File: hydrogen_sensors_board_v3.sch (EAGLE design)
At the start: 97 parts, among them CN1 1X4-CLEANBIG, IC1 317T, IC2 LM741D, U1 ATMEGA328P_TQFP, Y1 16MHz

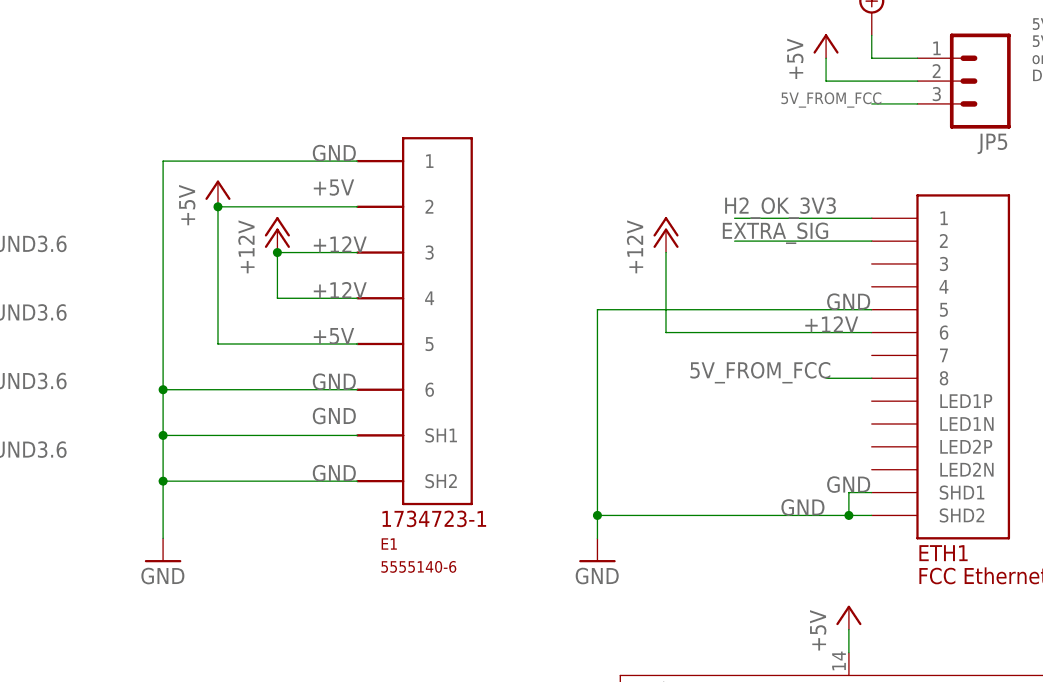
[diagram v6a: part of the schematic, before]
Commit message: updated rj 11 part. added signals to ethernet connector
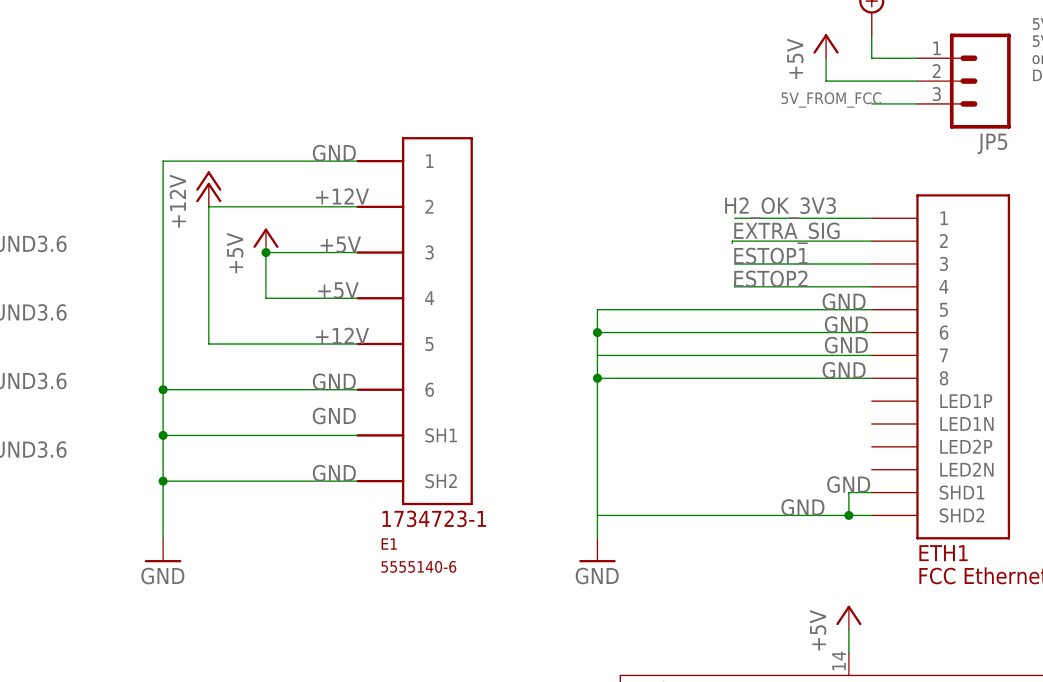
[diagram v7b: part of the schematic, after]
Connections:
- net +12V: now also E1.2, E1.5; no longer E1.3, E1.4, ETH1.6
- net +5V: now also E1.3, E1.4; no longer E1.2, E1.5
- net 5V_FROM_FCC: no longer ETH1.8
- net ESTOP1: now also ETH1.3
- net ESTOP2: now also ETH1.4
- net GND: now also ETH1.6, ETH1.7, ETH1.8
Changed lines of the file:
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@@
 <?xml version="1.0" encoding="utf-8"?>
 <!DOCTYPE eagle SYSTEM "eagle.dtd">
-<eagle version="7.6.0">
+<eagle version="9.1.0">
 <drawing>
 <settings>
 <setting alwaysvectorfont="no"/>
+<setting keepoldvectorfont="yes"/>
 <setting verticaltext="up"/>
 </settings>
-<grid distance="0.1" unitdist="inch" unit="inch" style="lines" multiple="1" display="no" altdistance="0.01" altunitdist="inch" altunit="inch"/>
+<grid distance="0.01" unitdist="inch" unit="inch" style="lines" multiple="1" display="no" altdistance="0.01" altunitdist="inch" altunit="inch"/>
 <layers>
 <layer number="1" name="Top" color="4" fill="1" visible="no" active="no"/>
@@
 <part name="P+14" library="supply1" deviceset="+5V" device=""/>
 <part name="P+15" library="supply1" deviceset="+5V" device=""/>
-<part name="P+17" library="supply1" deviceset="+12V" device=""/>
 <part name="GND14" library="SparkFun" deviceset="GND" device=""/>
-<part name="P+18" library="supply1" deviceset="+5V" device=""/>
 <part name="P+19" library="supply1" deviceset="+12V" device=""/>
 <part name="GND15" library="supply1" deviceset="GND" device=""/>
@@
 <part name="D1" library="adafruit" deviceset="DIODE" device="SMA" value="S1GTR"/>
 <part name="D2" library="adafruit" deviceset="DIODE" device="SMA" value="S1GTR"/>
+<part name="P+23" library="supply1" deviceset="+5V" device=""/>
 </parts>
 <sheets>
@@
 <instance part="P+14" gate="1" x="509.778" y="155.194"/>
 <instance part="P+15" gate="1" x="509.27" y="139.7"/>
-<instance part="P+17" gate="1" x="434.34" y="146.05"/>
 <instance part="GND14" gate="1" x="378.46" y="109.22"/>
-<instance part="P+18" gate="1" x="384.556" y="151.384"/>
-<instance part="P+19" gate="1" x="391.16" y="146.05"/>
+<instance part="P+19" gate="1" x="383.54" y="151.13"/>
 <instance part="GND15" gate="1" x="63.5" y="270.256"/>
 <instance part="GND16" gate="1" x="50.8" y="295.656"/>
@@
 <attribute name="VALUE" x="54.864" y="340.614" size="1.27" layer="96"/>
 </instance>
+<instance part="P+23" gate="1" x="389.89" y="146.05"/>
 </instances>
 <busses>
@@
 <wire x1="463.55" y1="356.87" x2="454.66" y2="356.87" width="0.1524" layer="91"/>
 <wire x1="454.66" y1="356.87" x2="454.66" y2="360.68" width="0.1524" layer="91"/>
-</segment>
-<segment>
-<pinref part="P+18" gate="1" pin="+5V"/>
-<wire x1="384.556" y1="148.844" x2="384.556" y2="148.59" width="0.1524" layer="91"/>
-<pinref part="E1" gate="G$1" pin="5"/>
-<label x="394.97" y="133.35" size="1.778" layer="95"/>
-<wire x1="384.556" y1="148.59" x2="384.556" y2="133.35" width="0.1524" layer="91"/>
-<wire x1="384.556" y1="133.35" x2="400.05" y2="133.35" width="0.1524" layer="91"/>
-<pinref part="E1" gate="G$1" pin="2"/>
-<label x="394.97" y="149.86" size="1.778" layer="95"/>
-<wire x1="400.05" y1="148.59" x2="384.556" y2="148.59" width="0.1524" layer="91"/>
-<junction x="384.556" y="148.59"/>
 </segment>
 <segment>
@@
 <junction x="53.34" y="113.284"/>
 </segment>
+<segment>
+<pinref part="E1" gate="G$1" pin="3"/>
+<wire x1="389.89" y1="143.51" x2="400.05" y2="143.51" width="0.1524" layer="91"/>
+<pinref part="E1" gate="G$1" pin="4"/>
+<wire x1="400.05" y1="138.43" x2="389.89" y2="138.43" width="0.1524" layer="91"/>
+<wire x1="389.89" y1="138.43" x2="389.89" y2="143.51" width="0.1524" layer="91"/>
+<pinref part="P+23" gate="1" pin="+5V"/>
+<junction x="389.89" y="143.51"/>
+<label x="395.732" y="143.51" size="1.778" layer="95"/>
+<label x="395.478" y="138.43" size="1.778" layer="95"/>
+</segment>
 </net>
 <net name="GND" class="0">
@@
 <segment>
 <pinref part="GND7" gate="1" pin="GND"/>
-<wire x1="426.72" y1="137.16" x2="426.72" y2="114.3" width="0.1524" layer="91"/>
+<pinref part="ETH1" gate="G$1" pin="SHD1"/>
 <wire x1="426.72" y1="114.3" x2="426.72" y2="111.76" width="0.1524" layer="91"/>
-<pinref part="ETH1" gate="G$1" pin="SHD1"/>
 <wire x1="457.2" y1="116.84" x2="454.66" y2="116.84" width="0.1524" layer="91"/>
 <wire x1="454.66" y1="116.84" x2="454.66" y2="114.3" width="0.1524" layer="91"/>
@@
 <junction x="454.66" y="114.3"/>
 <wire x1="454.66" y1="114.3" x2="426.72" y2="114.3" width="0.1524" layer="91"/>
-<junction x="426.72" y="114.3"/>
+<label x="452.12" y="116.84" size="1.778" layer="95"/>
+<label x="447.04" y="114.3" size="1.778" layer="95"/>
+<pinref part="ETH1" gate="G$1" pin="8"/>
+<wire x1="457.2" y1="129.54" x2="426.72" y2="129.54" width="0.1524" layer="91"/>
+<wire x1="426.72" y1="129.54" x2="426.72" y2="114.3" width="0.1524" layer="91"/>
+<pinref part="ETH1" gate="G$1" pin="7"/>
+<wire x1="457.2" y1="132.08" x2="426.72" y2="132.08" width="0.1524" layer="91"/>
+<junction x="426.72" y="129.54"/>
+<pinref part="ETH1" gate="G$1" pin="6"/>
+<wire x1="426.72" y1="132.08" x2="426.72" y2="129.54" width="0.1524" layer="91"/>
+<wire x1="457.2" y1="134.62" x2="426.72" y2="134.62" width="0.1524" layer="91"/>
+<wire x1="426.72" y1="134.62" x2="426.72" y2="132.08" width="0.1524" layer="91"/>
 <pinref part="ETH1" gate="G$1" pin="5"/>
 <wire x1="457.2" y1="137.16" x2="426.72" y2="137.16" width="0.1524" layer="91"/>
-<label x="452.12" y="137.16" size="1.778" layer="95"/>
-<label x="452.12" y="116.84" size="1.778" layer="95"/>
-<label x="447.04" y="114.3" size="1.778" layer="95"/>
+<wire x1="426.72" y1="137.16" x2="426.72" y2="134.62" width="0.1524" layer="91"/>
+<junction x="426.72" y="134.62"/>
+<label x="451.612" y="137.16" size="1.778" layer="95"/>
+<label x="451.866" y="134.62" size="1.778" layer="95"/>
+<label x="451.866" y="132.334" size="1.778" layer="95"/>
+<label x="451.612" y="129.54" size="1.778" layer="95"/>
 </segment>
 <segment>
@@
 <net name="EXTRA_SIG" class="0">
 <segment>
-<pinref part="ETH1" gate="G$1" pin="2"/>
-<label x="440.436" y="145.034" size="1.778" layer="95"/>
-<wire x1="457.2" y1="144.78" x2="441.96" y2="144.78" width="0.1524" layer="91"/>
-</segment>
-<segment>
 <pinref part="R25" gate="G$1" pin="2"/>
 <pinref part="R26" gate="G$1" pin="2"/>
@@
 <label x="485.14" y="334.264" size="1.27" layer="95"/>
 </segment>
+<segment>
+<pinref part="ETH1" gate="G$1" pin="2"/>
+<wire x1="457.2" y1="144.78" x2="441.706" y2="144.78" width="0.1524" layer="91"/>
+<wire x1="441.706" y1="144.78" x2="441.706" y2="144.526" width="0.1524" layer="91"/>
+<label x="441.706" y="145.034" size="1.778" layer="95"/>
+</segment>
 </net>
 <net name="RXD" class="0">
@@
 <label x="408.94" y="88.9" size="1.016" layer="95"/>
 </segment>
+<segment>
+<pinref part="ETH1" gate="G$1" pin="3"/>
+<wire x1="457.2" y1="142.24" x2="441.96" y2="142.24" width="0.1524" layer="91"/>
+<label x="441.706" y="142.24" size="1.778" layer="95"/>
+</segment>
 </net>
 <net name="ESTOP2" class="0">
@@
 <pinref part="U$8" gate="G$1" pin="1B"/>
 <label x="408.94" y="86.36" size="1.016" layer="95"/>
+</segment>
+<segment>
+<pinref part="ETH1" gate="G$1" pin="4"/>
+<wire x1="457.2" y1="139.7" x2="441.96" y2="139.7" width="0.1524" layer="91"/>
+<wire x1="441.96" y1="139.7" x2="441.96" y2="140.208" width="0.1524" layer="91"/>
+<label x="441.706" y="139.7" size="1.778" layer="95"/>
 </segment>
 </net>
@@
 <junction x="510.54" y="109.22"/>
 <pinref part="P+12" gate="1" pin="+12V"/>
-</segment>
-<segment>
-<pinref part="ETH1" gate="G$1" pin="6"/>
-<label x="449.58" y="134.62" size="1.778" layer="95"/>
-<pinref part="P+17" gate="1" pin="+12V"/>
-<wire x1="457.2" y1="134.62" x2="434.34" y2="134.62" width="0.1524" layer="91"/>
-<wire x1="434.34" y1="134.62" x2="434.34" y2="143.51" width="0.1524" layer="91"/>
-</segment>
-<segment>
-<pinref part="P+19" gate="1" pin="+12V"/>
-<wire x1="391.16" y1="143.51" x2="391.16" y2="138.43" width="0.1524" layer="91"/>
-<pinref part="E1" gate="G$1" pin="4"/>
-<wire x1="400.05" y1="138.43" x2="391.16" y2="138.43" width="0.1524" layer="91"/>
-<label x="394.97" y="138.43" size="1.778" layer="95"/>
-<pinref part="E1" gate="G$1" pin="3"/>
-<wire x1="400.05" y1="143.51" x2="391.16" y2="143.51" width="0.1524" layer="91"/>
-<label x="394.97" y="143.51" size="1.778" layer="95"/>
-<junction x="391.16" y="143.51"/>
 </segment>
 <segment>
@@
 <wire x1="124.46" y1="333.248" x2="124.46" y2="330.2" width="0.1524" layer="91"/>
 <pinref part="P+16" gate="1" pin="+12V"/>
+</segment>
+<segment>
+<pinref part="E1" gate="G$1" pin="2"/>
+<pinref part="P+19" gate="1" pin="+12V"/>
+<wire x1="400.05" y1="148.59" x2="383.54" y2="148.59" width="0.1524" layer="91"/>
+<pinref part="E1" gate="G$1" pin="5"/>
+<wire x1="400.05" y1="133.35" x2="383.54" y2="133.35" width="0.1524" layer="91"/>
+<wire x1="383.54" y1="133.35" x2="383.54" y2="148.59" width="0.1524" layer="91"/>
+<label x="395.224" y="133.35" size="1.778" layer="95"/>
+<label x="395.224" y="148.844" size="1.778" layer="95"/>
 </segment>
 </net>
@@
 <net name="5V_FROM_FCC" class="0">
 <segment>
-<pinref part="ETH1" gate="G$1" pin="8"/>
-<label x="436.88" y="129.54" size="1.778" layer="95"/>
-<wire x1="457.2" y1="129.54" x2="452.12" y2="129.54" width="0.1524" layer="91"/>
-</segment>
-<segment>
 <wire x1="462.28" y1="160.02" x2="457.2" y2="160.02" width="0.1524" layer="91"/>
